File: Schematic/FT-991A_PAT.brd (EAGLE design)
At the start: 44.6 x 59.8 mm, 33 parts, among them Q1 PE4259, Q2 MC78L09ABDR2GOSCT, Q5 NCP553, Q7 J310, Q8 5086, X1 IF_IN, X2 SCP_OUT, X3 SDR_OUT

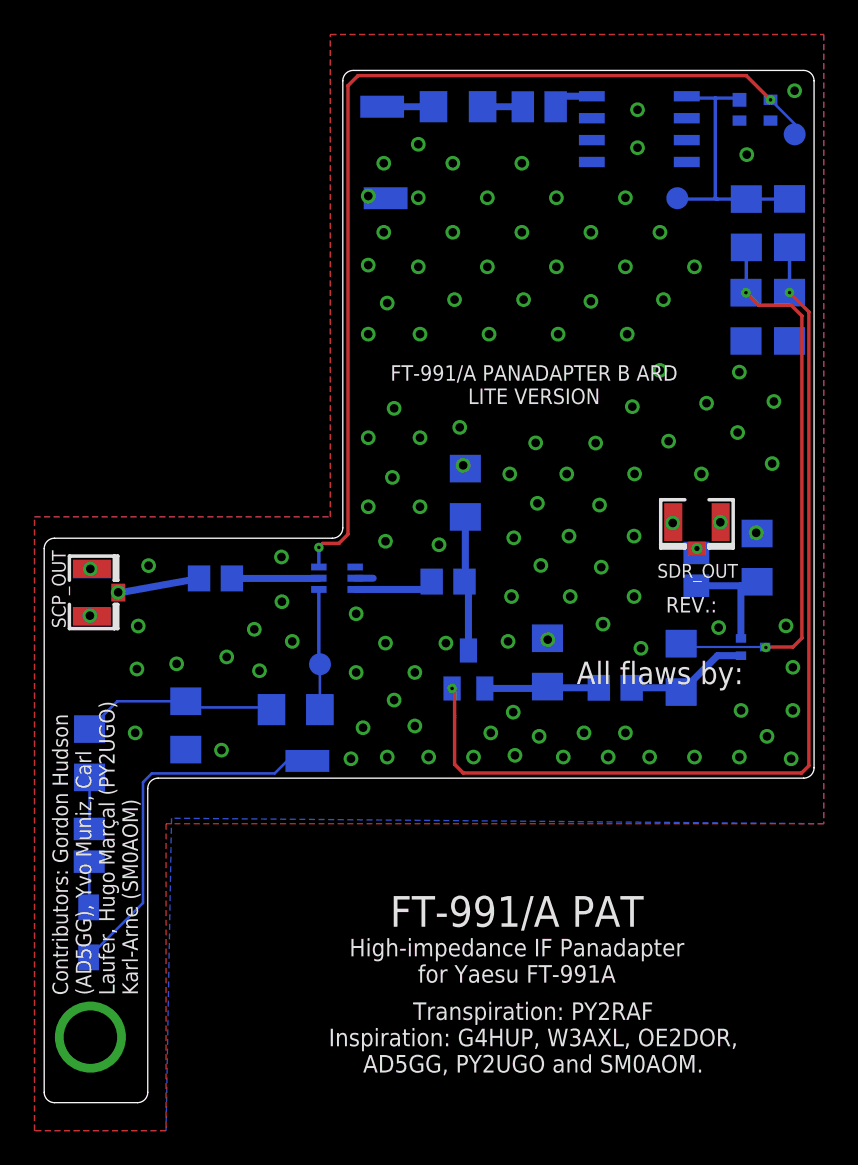
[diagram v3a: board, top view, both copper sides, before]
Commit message: Few more enhancements and impedance control
* Larger ground exposed ground pad near at the screw
* Changed pad for RF components to a rounded layout
* Enlarged the RF wire signal, in order to reduce the internal signal
  impedance
* Better component silk screen
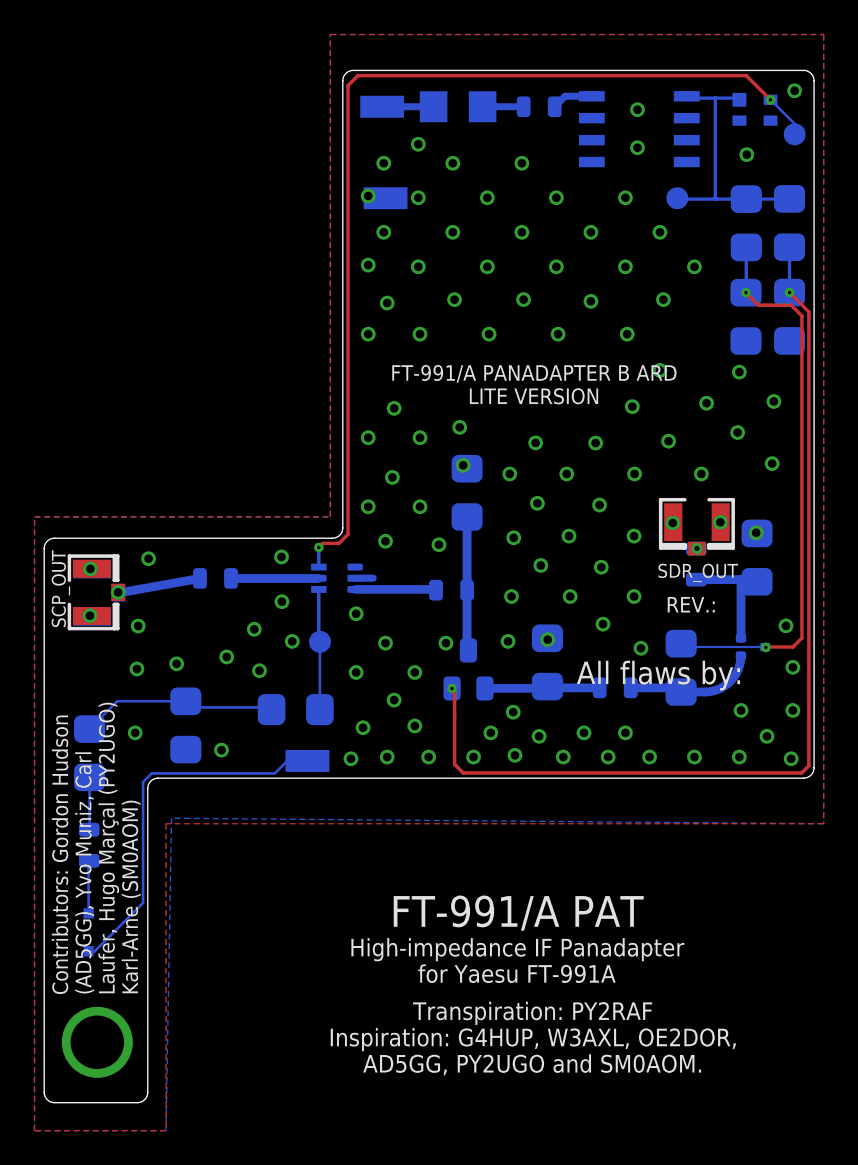
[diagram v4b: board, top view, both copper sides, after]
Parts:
- C1, C10, C13, C6: device rcl:C0805 -> aarf:0805
- C11, C7: device rcl:C3216 -> aarf:1206
- D1: device diode:SOD323-W -> aarf:SOD-323
- L2, L3: device rcl-modified:L0805 -> aarf:0805
- R10, R2, R3, R4, R5, R6, R7, R8, R9: device rcl:R3216 -> aarf:1206
- moved TP3 1.30 mm to (22.3, 38.3)
- moved C6 0.54 mm to (29.9, 41.3)
- moved C13 0.30 mm to (44.1, 42.8)
- moved R5 0.10 mm to (30.8, 46.9)
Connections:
- net FINAL: now also C13.P$2; no longer C13.2
- net IFIN: now also C6.P$1; no longer C6.1
- net IFTAP: now also C1.P$2; no longer C1.2
- net N$1: now also C13.P$1; no longer C13.1
- net N$25: now also L3.P$2; no longer L3.2
- net N$26: now also L2.P$1; no longer L2.1
- net N$32: now also L2.P$2; no longer L2.2
- net N$35: now also L3.P$1; no longer L3.1
- net N$4: now also C10.P$2; no longer C10.2
- net N$5: now also C10.P$1; no longer C10.1
- net N$6: now also C6.P$2; no longer C6.2
- net RAWIN: now also C1.P$1; no longer C1.1
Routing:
- net N$1: track 6.67 -> 7.30 mm
- net GNDA: vias 120 -> 119

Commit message: Rev. Q: Rew improvements
* Moved TX9 signal treatment compoments from board lid to larger board
* Changed fuse silk screen
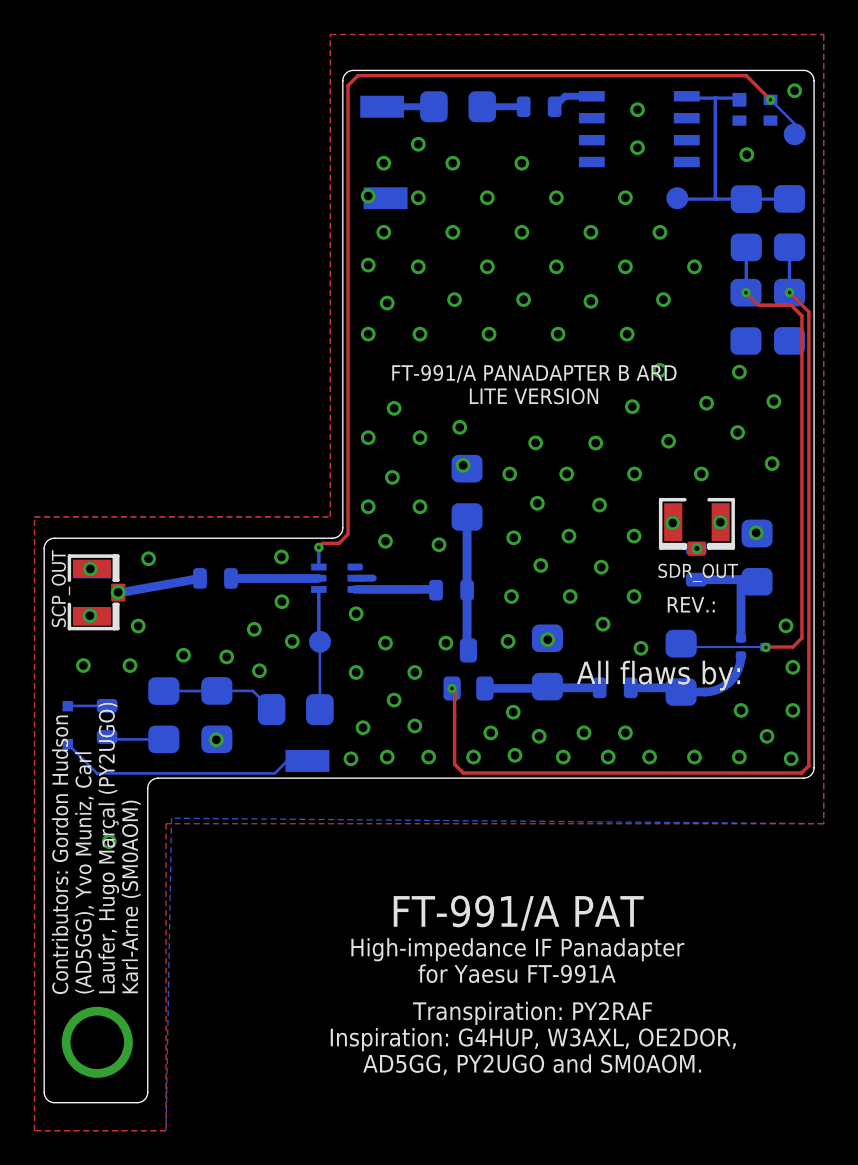
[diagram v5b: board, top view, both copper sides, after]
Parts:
- F1: device adafruit:R1206 -> aarf:FUSE-1206
- moved D1 12.1 mm to (7.70, 33.5)
- moved L3 7.25 mm to (9.97, 33.7), turned to 270 degrees
- moved R3 4.83 mm to (13.3, 34.0)
- moved R4 1.90 mm to (16.3, 34.1)
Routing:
- net N$18: track 21.3 -> 14.9 mm
- net N$8: track 11.6 -> 6.87 mm
- net N$35: track 3.06 -> 2.28 mm
- net GNDA: vias 119 -> 120
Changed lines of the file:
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@@
 <text x="32.3" y="53.8" size="1" layer="30" font="vector" ratio="15" rot="MR0" align="center">VAI CORINTHIANS!</text>
 <text x="42" y="36.5" size="1.3" layer="21" font="vector" ratio="15" rot="R180" align="center">All flaws by:</text>
-<wire x1="29.2" y1="69.3" x2="31.2" y2="69.3" width="0.1524" layer="22"/>
 <text x="14.7" y="39.8" size="1.3" layer="29" font="vector" ratio="15" rot="R180" align="center">Light
 Ed</text>
@@
 <attribute name="VALUE" x="7.56911875" y="41.346790625" size="0.8" layer="21" font="vector" ratio="15" rot="R270" align="top-center"/>
 </element>
-<element name="D1" library="aarf" package="SOD-323" value="1SS355VM" x="8.89535625" y="21.470890625" smashed="yes" rot="MR270"/>
+<element name="D1" library="aarf" package="SOD-323" value="1SS355VM" x="7.69535625" y="33.470890625" smashed="yes" rot="MR270"/>
 <element name="PAD3" library="wirepad" library_urn="urn:adsk.eagle:library:412" package="SMD1,27-2,54" package3d_urn="urn:adsk.eagle:package:30839/1" value="TX9" x="21.5685125" y="31.400603125" smashed="yes" rot="MR270">
 <attribute name="VALUE" x="18.6635125" y="31.065603125" size="0.8" layer="22" font="vector" ratio="15" rot="MR180" align="top-center"/>
@@
 <attribute name="VALUE" x="36.67" y="67.36" size="0.8" layer="22" font="vector" ratio="15" rot="MR0"/>
 </element>
-<element name="R4" library="aarf" package="1206" value="5.6kΩ" x="14.526321875" y="33.454659375" smashed="yes" rot="MR270">
-<attribute name="VALUE" x="12.966321875" y="33.489659375" size="0.8" layer="22" font="vector" ratio="15" rot="MR270" align="center"/>
-</element>
-<element name="R3" library="aarf" package="1206" value="10kΩ" x="8.9510625" y="31.847921875" smashed="yes" rot="MR270">
-<attribute name="VALUE" x="7.6910625" y="33.082921875" size="0.8" layer="22" font="vector" ratio="15" rot="MR270"/>
-</element>
-<element name="L3" library="aarf" package="0805" value="BLM21" x="8.9338" y="26.51251875" smashed="yes" rot="MR90">
-<attribute name="VALUE" x="6.8938" y="24.84251875" size="0.8" layer="22" font="vector" ratio="15" rot="MR90"/>
+<element name="R4" library="aarf" package="1206" value="5.6kΩ" x="16.326321875" y="34.054659375" smashed="yes" rot="MR270">
+<attribute name="VALUE" x="14.766321875" y="34.089659375" size="0.8" layer="22" font="vector" ratio="15" rot="MR270" align="center"/>
+</element>
+<element name="R3" library="aarf" package="1206" value="10kΩ" x="13.2510625" y="34.047921875" smashed="yes" rot="MR270">
+<attribute name="VALUE" x="11.9910625" y="35.282921875" size="0.8" layer="22" font="vector" ratio="15" rot="MR270"/>
+</element>
+<element name="L3" library="aarf" package="0805" value="BLM21" x="9.9662" y="33.68748125" smashed="yes" rot="MR270">
+<attribute name="VALUE" x="10.3062" y="32.15748125" size="0.8" layer="22" font="vector" ratio="15" rot="MR270"/>
 </element>
 <element name="C13" library="aarf" package="0805" value="1000pF" x="44.1" y="42.8" smashed="yes" rot="MR90">
@@
 <attribute name="VALUE" x="46.84" y="70.76" size="0.8" layer="22" font="vector" ratio="15" rot="MR0" align="center"/>
 </element>
-<element name="F1" library="adafruit" package="R1206" value="50mA" x="30.3" y="69.3" smashed="yes" rot="MR180">
+<element name="F1" library="aarf" package="FUSE-1206" value="50mA" x="30.3" y="69.3" smashed="yes" rot="MR180">
 <attribute name="VALUE" x="30.303" y="67.513" size="0.8" layer="22" font="vector" ratio="15" rot="MR180" align="center"/>
 </element>
@@
 <via x="16.895" y="37.425" extent="1-16" drill="0.5"/>
 <via x="20.095" y="40.625" extent="1-16" drill="0.5"/>
-<via x="13.995" y="37.025" extent="1-16" drill="0.5"/>
+<via x="14.395" y="37.525" extent="1-16" drill="0.5"/>
 <via x="24.395" y="39.925" extent="1-16" drill="0.5"/>
-<via x="16.595" y="32.025" extent="1-16" drill="0.5"/>
+<via x="10.095" y="26.725" extent="1-16" drill="0.5"/>
 <via x="18.495" y="39.025" extent="1-16" drill="0.5"/>
-<via x="11.595" y="33.025" extent="1-16" drill="0.5"/>
-<via x="11.695" y="36.725" extent="1-16" drill="0.5"/>
+<via x="8.595" y="36.925" extent="1-16" drill="0.5"/>
+<via x="11.295" y="36.925" extent="1-16" drill="0.5"/>
 <via x="46.595" y="31.625" extent="1-16" drill="0.5"/>
 <via x="43.995" y="31.625" extent="1-16" drill="0.5"/>
@@
 <via x="20.695" y="38.325" extent="1-16" drill="0.5"/>
 <contactref element="GND" pad="1"/>
+<via x="16.295" y="32.625" extent="1-16" drill="0.5"/>
 <wire x1="24.395" y1="39.925" x2="24.335" y2="41.985" width="0" layer="19" extent="16-16"/>
 <wire x1="8.995" y1="42.525" x2="9.08411875" y2="42.541790625" width="0" layer="19" extent="1-1"/>
@@
 <contactref element="13.8V" pad="1"/>
 <contactref element="F1" pad="1"/>
-<wire x1="25.9" y1="69.3" x2="28.878" y2="69.3" width="0.4064" layer="16"/>
+<wire x1="25.9" y1="69.3" x2="28.9" y2="69.3" width="0.4064" layer="16"/>
 </signal>
 <signal name="N$26">
@@
 <wire x1="21.5685125" y1="31.400603125" x2="20.400603125" y2="31.400603125" width="0.15" layer="16"/>
 <wire x1="20.400603125" y1="31.400603125" x2="19.6775" y2="30.6775" width="0.15" layer="16"/>
-<wire x1="12.5553375" y1="30.6775" x2="12.0475" y2="30.1696625" width="0.15" layer="16"/>
-<wire x1="19.6775" y1="30.6775" x2="12.5553375" y2="30.6775" width="0.15" layer="16"/>
-<wire x1="12.0475" y1="30.1696625" x2="12.0475" y2="23.173034375" width="0.15" layer="16"/>
-<wire x1="12.0475" y1="23.173034375" x2="9.24535625" y2="20.370890625" width="0.15" layer="16"/>
-<wire x1="9.24535625" y1="20.370890625" x2="8.89535625" y2="20.370890625" width="0.15" layer="16"/>
+<wire x1="19.6775" y1="30.6775" x2="12.311253125" y2="30.6775" width="0.15" layer="16"/>
+<wire x1="12.311253125" y1="30.6775" x2="9.388746875" y2="30.6775" width="0.1524" layer="16"/>
+<wire x1="9.388746875" y1="30.6775" x2="7.69535625" y2="32.370890625" width="0.1524" layer="16"/>
 </signal>
 <signal name="N$35">
 <contactref element="D1" pad="C"/>
 <contactref element="L3" pad="P$1"/>
-<wire x1="8.89535625" y1="22.570890625" x2="8.89535625" y2="25.574075" width="0.15" layer="16"/>
-<wire x1="8.89535625" y1="25.574075" x2="8.9338" y2="25.61251875" width="0.15" layer="16"/>
+<wire x1="9.9662" y1="34.58748125" x2="7.711946875" y2="34.58748125" width="0.1524" layer="16"/>
+<wire x1="7.711946875" y1="34.58748125" x2="7.69535625" y2="34.570890625" width="0.1524" layer="16"/>
 </signal>
 <signal name="FINAL">
@@
 <contactref element="R4" pad="1"/>
 <contactref element="R2" pad="1"/>
-<wire x1="8.9510625" y1="33.247921875" x2="10.5578" y2="34.854659375" width="0.15" layer="16"/>
-<wire x1="10.5578" y1="34.854659375" x2="14.5" y2="34.854659375" width="0.15" layer="16"/>
-<wire x1="14.5" y1="34.854659375" x2="14.526321875" y2="34.854659375" width="0.15" layer="16"/>
 <wire x1="19.49288125" y1="34.37455625" x2="19.3674375" y2="34.5" width="0.15" layer="16"/>
-<wire x1="19.3674375" y1="34.5" x2="14.5" y2="34.5" width="0.15" layer="16"/>
-<wire x1="14.5" y1="34.5" x2="14.5" y2="34.854659375" width="0.15" layer="16"/>
+<wire x1="19.49288125" y1="34.37455625" x2="18.412778125" y2="35.454659375" width="0.1524" layer="16"/>
+<wire x1="18.412778125" y1="35.454659375" x2="16.326321875" y2="35.454659375" width="0.1524" layer="16"/>
+<wire x1="13.2510625" y1="35.447921875" x2="16.319584375" y2="35.447921875" width="0.1524" layer="16"/>
+<wire x1="16.319584375" y1="35.447921875" x2="16.326321875" y2="35.454659375" width="0.1524" layer="16"/>
 </signal>
 <signal name="N$25">
 <contactref element="L3" pad="P$2"/>
 <contactref element="R3" pad="2"/>
-<wire x1="8.9338" y1="27.41251875" x2="8.9510625" y2="27.47978125" width="0.15" layer="16"/>
-<wire x1="8.9510625" y1="27.47978125" x2="8.9510625" y2="30.447921875" width="0.15" layer="16"/>
+<wire x1="13.2510625" y1="32.647921875" x2="13.22336875" y2="32.647921875" width="0.15" layer="16"/>
+<wire x1="13.2510625" y1="32.647921875" x2="10.105759375" y2="32.647921875" width="0.1524" layer="16"/>
+<wire x1="10.105759375" y1="32.647921875" x2="9.9662" y2="32.78748125" width="0.1524" layer="16"/>
 </signal>
 <signal name="N$32">
 <contactref element="L2" pad="P$2"/>
 <contactref element="F1" pad="2"/>
-<wire x1="31.722" y1="69.3" x2="34.1" y2="69.3" width="0.4064" layer="16"/>
+<wire x1="31.7" y1="69.3" x2="34.1" y2="69.3" width="0.4064" layer="16"/>
 </signal>
 <signal name="IFTAP">

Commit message: Starring: Revision R
Check CHANGELOG.md file.
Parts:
- removed C6: 1000pF, aarf:0805
- removed R6: 220Ω, aarf:1206
- removed R9: 1kΩ, aarf:1206
- moved TP1 4.63 mm to (47.5, 62.9)
- moved Q1 3.67 mm to (26.9, 41.3)
- moved C1 0.85 mm to (16.5, 41.2)
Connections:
- removed net 9V5086: C11.1, Q8.3, R8.1, R9.2
- removed net 9VJ310: C7.1, Q7.2, R6.1
- removed net N$6: C6.P$2, Q7.3, R5.2
- net 3V: now also C11.1, Q8.3, R8.1
- net 9V: now also C7.1, Q7.2; no longer R6.2, R9.1
- net IFIN: now also Q7.3, R5.2; no longer C6.P$1
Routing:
- net 9VJ310: track 55.9 -> 0.00 mm, vias 2 -> 0
- net 9V: track 15.6 -> 69.3 mm, vias 0 -> 2
- net 3V: track 57.0 -> 98.5 mm, vias 2 -> 4
- net 9V5086: track 32.4 -> 0.00 mm, vias 2 -> 0
- net N$6: track 7.91 -> 0.00 mm
- net IFIN: track 4.71 -> 10.7 mm
- net IFTAP: track 5.10 -> 8.44 mm
- net N$7: track 6.99 -> 9.15 mm
- net GNDA: track 1.05 -> 0.00 mm, vias 120 -> 127
